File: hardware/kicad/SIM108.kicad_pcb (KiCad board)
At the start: 2 copper layers, 100 x 85 mm, 98 parts, among them J1 Screw_Terminal_01x09, J2 CAN, Q1 BC547, Q10 BC337-40, Q11 BC547, Q12 BC337-40, Q13 BC547, Q14 BC337-40, Q15 BC547, Q16 BC337-40, Q2 BC337-40, Q3 BC547, Q4 BC337-40, Q5 BC547, Q6 BC337-40, Q7 BC547, Q8 BC337-40, Q9 BC547, SW1 PRG, SW2 INSTANCE, SW3 BUS, U1 MCP2551-I-P, U10 SFH617A-1, U12 SFH617A-1, U14 SFH617A-1, U16 SFH617A-1, U18 SFH617A-1, U2 TMR_2411, U20 SFH617A-1, U4 74HC595, U5 Teensy_4.0, U6 SFH617A-1, U8 SFH617A-1

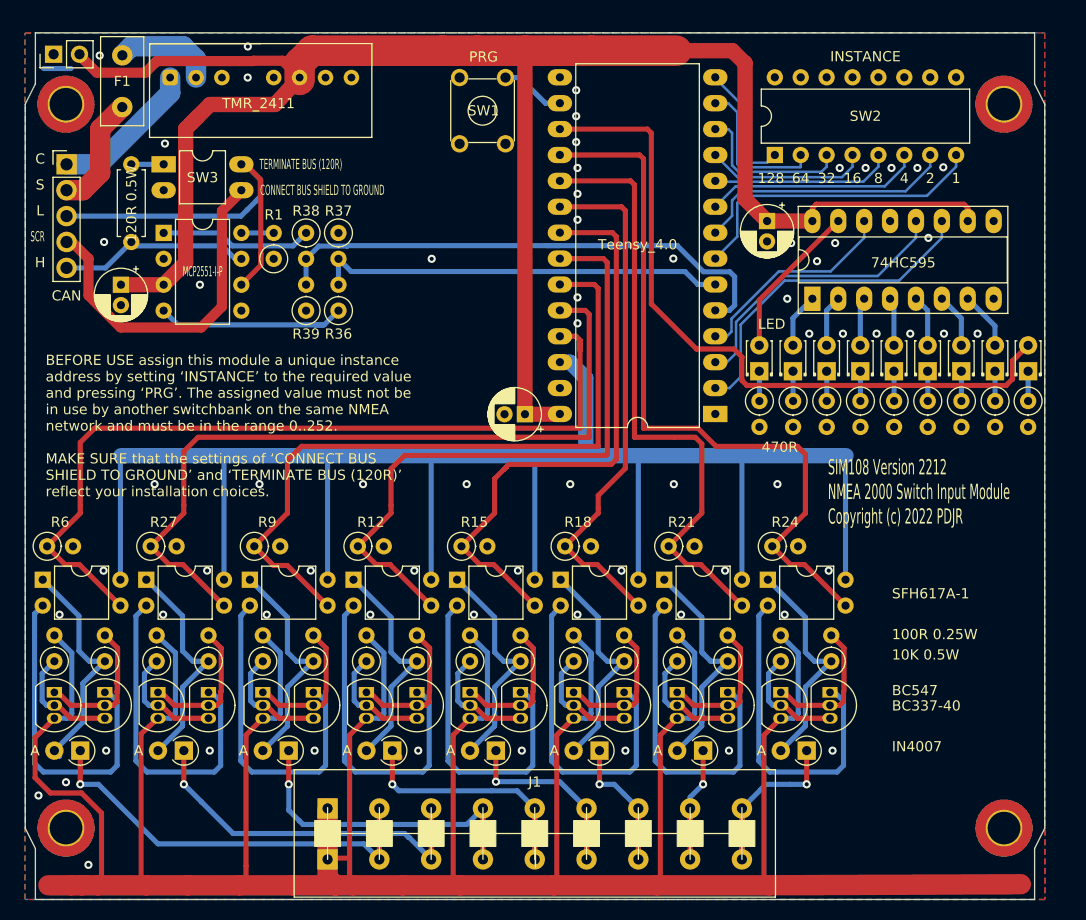
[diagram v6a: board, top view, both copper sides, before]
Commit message: Move to SMD
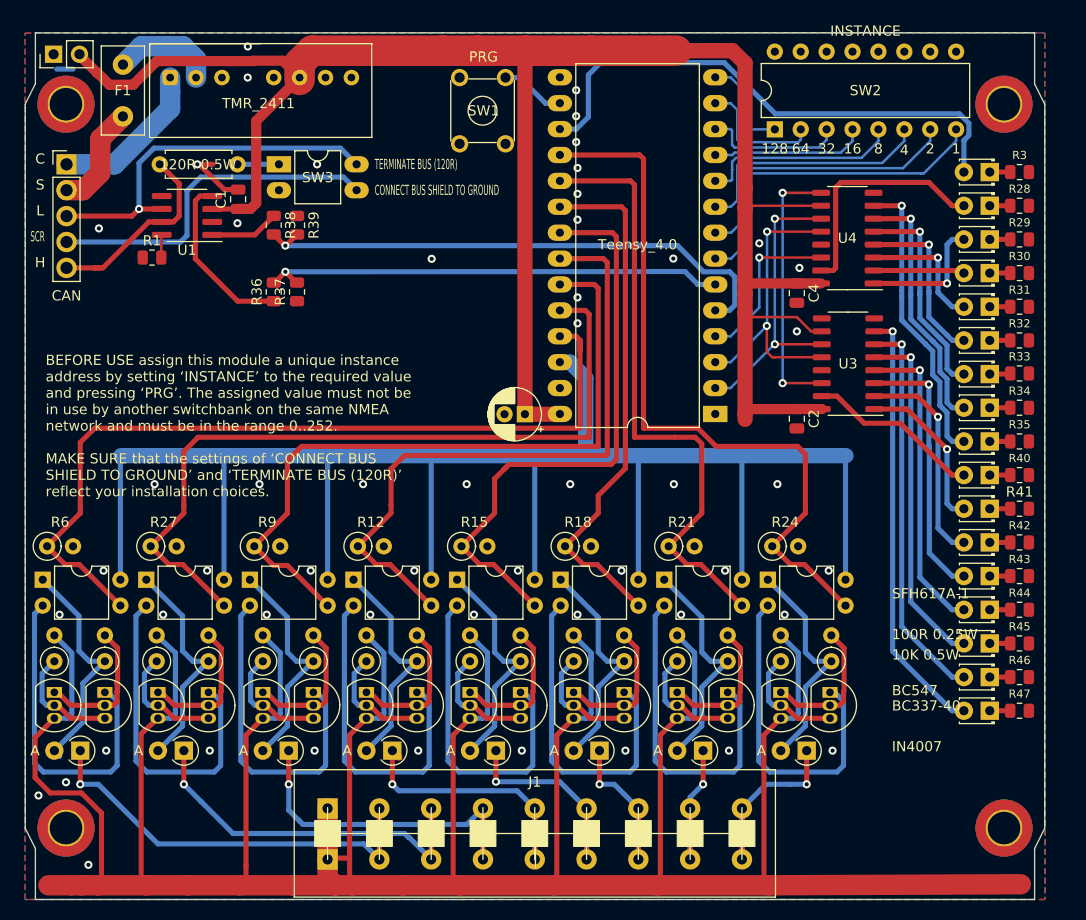
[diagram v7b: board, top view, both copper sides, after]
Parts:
- added C2: 100nF, Capacitor_SMD:C_0805_2012Metric, F.Cu at (95.7, 57.8)
- added D18: LED, LED_THT:LED_D1.8mm_W3.3mm_H2.4mm, F.Cu at (114.6, 63.4)
- added D19: LED, LED_THT:LED_D1.8mm_W3.3mm_H2.4mm, F.Cu at (114.6, 70.0)
- added D20: LED, LED_THT:LED_D1.8mm_W3.3mm_H2.4mm, F.Cu at (114.6, 76.6)
- added D21: LED, LED_THT:LED_D1.8mm_W3.3mm_H2.4mm, F.Cu at (114.6, 83.2)
- added D22: LED, LED_THT:LED_D1.8mm_W3.3mm_H2.4mm, F.Cu at (114.6, 66.7)
- added D23: LED, LED_THT:LED_D1.8mm_W3.3mm_H2.4mm, F.Cu at (114.6, 73.3)
- added D24: LED, LED_THT:LED_D1.8mm_W3.3mm_H2.4mm, F.Cu at (114.6, 79.9)
- added D25: LED, LED_THT:LED_D1.8mm_W3.3mm_H2.4mm, F.Cu at (114.6, 86.5)
- added R40: 560R, Resistor_SMD:R_0805_2012Metric, F.Cu at (117.5, 63.4)
- added R41: 560R, Resistor_SMD:R_0805_2012Metric, F.Cu at (117.5, 66.7)
- added R42: 560R, Resistor_SMD:R_0805_2012Metric, F.Cu at (117.5, 70.0)
- added R43: 560R, Resistor_SMD:R_0805_2012Metric, F.Cu at (117.5, 73.3)
- added R44: 560R, Resistor_SMD:R_0805_2012Metric, F.Cu at (117.5, 76.6)
- added R45: 560R, Resistor_SMD:R_0805_2012Metric, F.Cu at (117.5, 79.9)
- added R46: 560R, Resistor_SMD:R_0805_2012Metric, F.Cu at (117.5, 83.2)
- added R47: 560R, Resistor_SMD:R_0805_2012Metric, F.Cu at (117.5, 86.5)
- added U3: 74HCT595, Package_SO:SO-16_3.9x9.9mm_P1.27mm, F.Cu at (100.7, 52.5)
- C1, C4: footprint Capacitor_THT:CP_Radial_D5.0mm_P2.00mm -> Capacitor_SMD:C_0805_2012Metric
- R1, R36, R37, R38, R39: footprint Resistor_THT:R_Axial_DIN0207_L6.3mm_D2.5mm_P2.54mm_Vertical -> Resistor_SMD:R_0805_2012Metric
- R28, R29, R3, R30, R31, R32, R33, R34, R35: value 470R -> 560R; footprint Resistor_THT:R_Axial_DIN0207_L6.3mm_D2.5mm_P2.54mm_Vertical -> Resistor_SMD:R_0805_2012Metric
- U1: footprint Package_DIP:DIP-8_W7.62mm -> Package_SO:SOIC-8_3.9x4.9mm_P1.27mm
- U4: value 74HC595 -> 74HCT595; footprint Package_DIP:DIP-16_W7.62mm_Socket_LongPads -> Package_SO:SO-16_3.9x9.9mm_P1.27mm
- moved R28 31.9 mm to (117.5, 37.0), turned to 0 degrees
- moved D1 27.8 mm to (114.6, 37.0), turned to 180 degrees
- moved R29 27.3 mm to (117.5, 40.3), turned to 0 degrees
- moved D6 23.2 mm to (114.6, 40.3), turned to 180 degrees
- moved R30 22.7 mm to (117.5, 43.6), turned to 0 degrees
- moved R3 22.5 mm to (117.5, 33.7), turned to 0 degrees
- moved D5 19.9 mm to (114.6, 33.7), turned to 180 degrees
- moved D2 18.7 mm to (114.6, 43.6), turned to 180 degrees
- moved R31 18.1 mm to (117.5, 46.9), turned to 0 degrees
- moved C1 14.2 mm to (40.9, 36.3), turned to 90 degrees
- moved D7 14.2 mm to (114.6, 46.9), turned to 180 degrees
- moved R32 13.7 mm to (117.5, 50.2), turned to 0 degrees
- moved R1 11.9 mm to (32.4, 42.0), turned to 0 degrees
- moved SW3 11.3 mm to (44.9, 32.9)
- moved D3 9.87 mm to (114.6, 50.2), turned to 180 degrees
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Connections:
- U4 pad 9: Net-(U4-Pad9) -> /MPX_SER
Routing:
- net Net-(D25-Pad2): track 0.00 -> 42.6 mm, vias 0 -> 1
- net Net-(D21-Pad2): track 0.00 -> 38.5 mm, vias 0 -> 1
- net Net-(D24-Pad2): track 0.00 -> 34.5 mm, vias 0 -> 1
- net Net-(D20-Pad2): track 0.00 -> 30.4 mm, vias 0 -> 1
- net Net-(D23-Pad2): track 0.00 -> 26.3 mm, vias 0 -> 1
- net /MPX_SER: track 0.00 -> 26.3 mm, vias 0 -> 2
- net Net-(D9-Pad2): track 5.68 -> 29.1 mm, vias 0 -> 1
- net Net-(D19-Pad2): track 0.00 -> 21.1 mm, vias 0 -> 1
- net Net-(D4-Pad2): track 6.00 -> 25.0 mm, vias 0 -> 1
- net /TRANSMIT_LED: track 70.2 -> 52.7 mm
- net Net-(D18-Pad2): track 0.00 -> 17.2 mm
- net Net-(D22-Pad2): track 0.00 -> 16.0 mm, vias 0 -> 1
- net Net-(D8-Pad2): track 5.05 -> 21.0 mm, vias 0 -> 1
- net +5V: track 185.6 -> 198.2 mm
- net Net-(D3-Pad2): track 4.73 -> 16.9 mm, vias 0 -> 1
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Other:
- board text removed: "SIM108 Version 2212 NMEA 2000 Switch Input Module Copyright (c) 2022 PDJR"

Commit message: SMD
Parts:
- removed TEST: PinHeader_1x02_P2.54mm_Vertical, Connector_PinHeader_2.54mm:PinHeader_1x02_P2.54mm_Vertical
- C3: footprint Capacitor_THT:CP_Radial_D5.0mm_P2.00mm -> Capacitor_SMD:C_0805_2012Metric
- D10, D11, D12, D13, D14, D15, D16, D17: footprint Diode_THT:D_A-405_P2.54mm_Vertical_AnodeUp -> Diode_SMD:D_SOT-23_ANK
- Q1, Q10, Q11, Q12, Q13, Q14, Q15, Q16, Q2, Q3, Q4, Q5, Q6, Q7, Q8, Q9: footprint Package_TO_SOT_THT:TO-92_Inline -> Package_TO_SOT_SMD:TSOT-23
- R10, R11, R12, R13, R14, R15, R16, R17, R18, R19, R20, R21, R22, R23, R24, R25, R26, R27, R4, R5, R6, R7, R8, R9: footprint Resistor_THT:R_Axial_DIN0207_L6.3mm_D2.5mm_P2.54mm_Vertical -> Resistor_SMD:R_0805_2012Metric
- U10, U12, U14, U16, U18, U20, U6, U8: footprint Package_DIP:DIP-4_W7.62mm -> Package_DIP:SMDIP-4_W7.62mm
- moved U18 9.07 mm to (101.9, 73.4), turned to 90 degrees
- moved J1 8.52 mm to (41.1, 100.7)
- moved U16 8.44 mm to (91.1, 73.4), turned to 90 degrees
- moved U14 7.80 mm to (80.3, 73.4), turned to 90 degrees
- moved U12 7.17 mm to (69.5, 73.4), turned to 90 degrees
- moved U10 6.47 mm to (58.7, 73.4), turned to 90 degrees
- moved Q13 6.03 mm to (100.1, 84.4)
- moved U8 5.83 mm to (47.9, 73.4), turned to 90 degrees
- moved D16 5.63 mm to (101.9, 88.4), turned to 270 degrees
- moved Q11 5.33 mm to (89.3, 84.4)
- moved U20 5.26 mm to (37.1, 73.4), turned to 90 degrees
- moved R23 5.22 mm to (99.2, 80.4)
- moved D15 4.98 mm to (91.0, 88.4), turned to 270 degrees
- moved Q14 4.76 mm to (103.7, 84.4)
- moved Q9 4.76 mm to (78.5, 84.4)
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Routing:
- net /SPST_GND: track 333.0 -> 64.6 mm, vias 0 -> 8
- net /3V3: track 182.4 -> 125.4 mm, vias 0 -> 8
- net Net-(Q16-Pad1): track 32.6 -> 6.47 mm
- net Net-(Q12-Pad1): track 32.5 -> 6.44 mm
- net Net-(Q14-Pad1): track 32.5 -> 6.47 mm
- net Net-(Q4-Pad1): track 32.5 -> 6.47 mm
- net Net-(Q8-Pad1): track 32.5 -> 6.47 mm
- net Net-(Q6-Pad1): track 32.5 -> 6.53 mm
- net Net-(Q2-Pad1): track 32.4 -> 6.47 mm
- net Net-(Q10-Pad1): track 32.5 -> 6.76 mm
- net +5V: track 198.2 -> 173.6 mm
- net /SPST_CH3: track 29.2 -> 12.5 mm, vias 1 -> 0
- net /SPST_CH2: track 31.1 -> 17.2 mm, vias 1 -> 0
- net /SPST_CH1: track 35.6 -> 23.0 mm, vias 1 -> 0
- net /SPST_CH0: track 40.7 -> 28.7 mm, vias 1 -> 0
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- added copper zone on B.Cu, net /SPST_GND
